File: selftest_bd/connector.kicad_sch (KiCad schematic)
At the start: 209 parts, among them J1 9001-14961C00A, J2 9001-14961C00A

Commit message: Commit V2.0
Redo PCB due to incorrect position of J1 and J2
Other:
- title: FIRST TEST STATION SELFTEST BOARD 640-1010-010 -> FIRST TEST STATION SELFTEST BOARD 640-1010-020
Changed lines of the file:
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@@
   (paper "A")
   (title_block
-    (title "FIRST TEST STATION SELFTEST BOARD 640-1010-010")
-    (date "2023-05-16")
-    (rev "1.0")
+    (title "FIRST TEST STATION SELFTEST BOARD 640-1010-020")
+    (date "2023-10-01")
+    (rev "2.0")
   )
   (junction (at 25.4 96.52) (diameter 0) (color 0 0 0 0)

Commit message: update README and small correction
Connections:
- net PM1_IO8 renamed PM1_IO0
- net PM1_IO9 renamed PM1_IO1
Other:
- title: FIRST TEST STATION SELFTEST BOARD 640-1010-020 -> FIRST TEST STATION SELFTEST BOARD 640-1010-021
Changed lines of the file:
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@@
   (paper "A")
   (title_block
-    (title "FIRST TEST STATION SELFTEST BOARD 640-1010-020")
+    (title "FIRST TEST STATION SELFTEST BOARD 640-1010-021")
     (date "2023-10-01")
-    (rev "2.0")
+    (rev "2.1")
   )
   (junction (at 25.4 96.52) (diameter 0) (color 0 0 0 0)
@@
     )
   )
-  (global_label "PM1_IO9" (shape bidirectional) (at 109.22 91.44 0) (fields_autoplaced)
-    (effects (font (size 1.27 1.27)) (justify left))
-    (property "Intersheetrefs" "${INTERSHEET_REFS}" (at 119.6764 91.3606 0)
+  (global_label "PM1_IO1" (shape bidirectional) (at 109.22 91.44 0) (fields_autoplaced)
+    (effects (font (size 1.27 1.27)) (justify left))
+    (property "Intersheetrefs" "${INTERSHEET_REFS}" (at 121.2804 91.44 0)
       (effects (font (size 1.27 1.27)) (justify left) hide)
     )
@@
     )
   )
-  (global_label "PM1_IO8" (shape bidirectional) (at 43.18 134.62 180) (fields_autoplaced)
-    (effects (font (size 1.27 1.27)) (justify right))
-    (property "Intersheetrefs" "${INTERSHEET_REFS}" (at 32.7236 134.5406 0)
-      (effects (font (size 1.27 1.27)) (justify right) hide)
-    )
+  (global_label "PM1_IO0" (shape bidirectional) (at 43.18 134.62 180) (fields_autoplaced)
+    (effects (font (size 1.27 1.27)) (justify right))
+    (property "Intersheetrefs" "${INTERSHEET_REFS}" (at 31.1196 134.62 0)
+      (effects (font (size 1.27 1.27)) (justify right) hide)
+    )

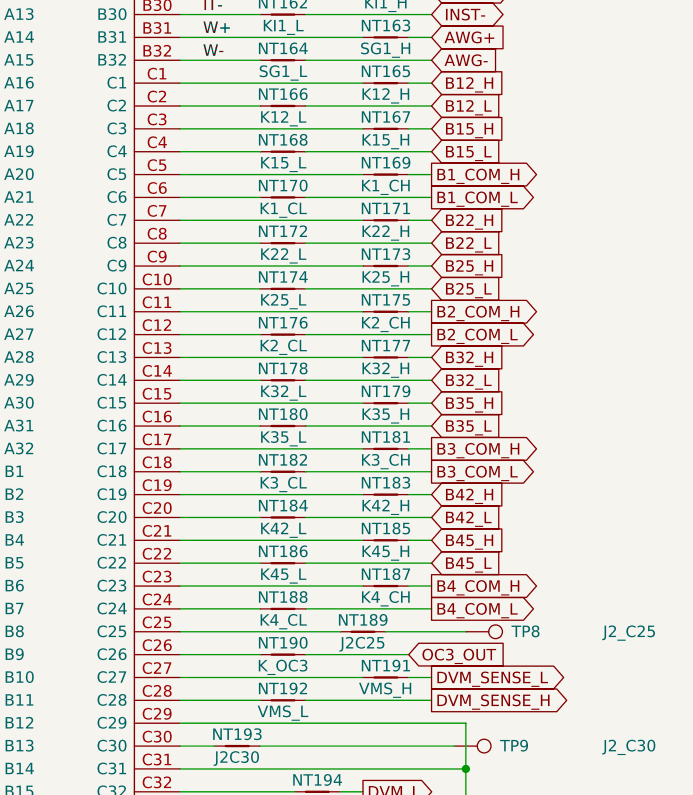
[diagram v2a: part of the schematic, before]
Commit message: Reverse COM_H and COM_L on relay Bank
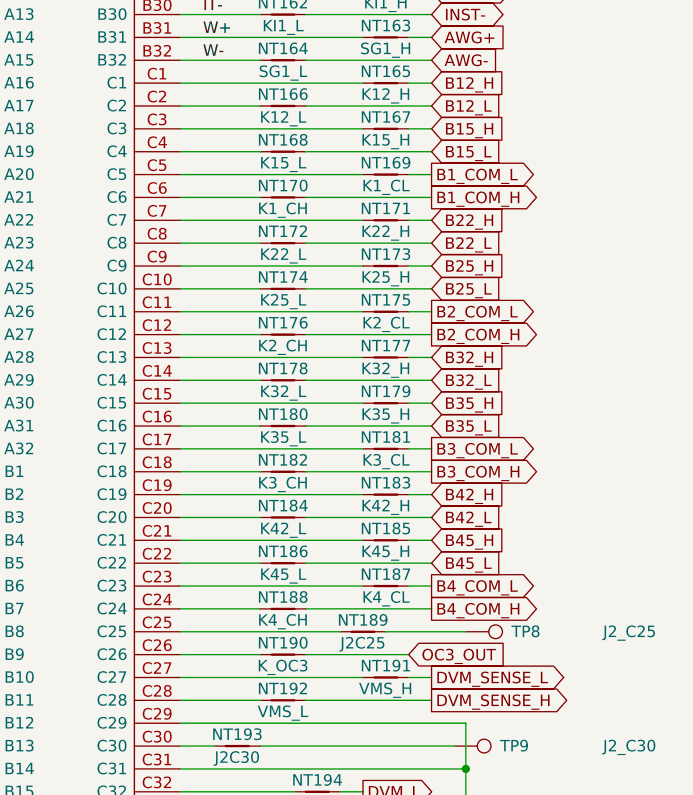
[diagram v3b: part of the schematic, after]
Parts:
- NT169: value K1_CH -> K1_CL
- NT170: value K1_CL -> K1_CH
- NT175: value K2_CH -> K2_CL
- NT176: value K2_CL -> K2_CH
- NT181: value K3_CH -> K3_CL
- NT182: value K3_CL -> K3_CH
- NT187: value K4_CH -> K4_CL
- NT188: value K4_CL -> K4_CH
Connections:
- net B1_COM_H: now also NT170.1; no longer NT169.1
- net B1_COM_L: now also NT169.1; no longer NT170.1
- net B2_COM_H: now also NT176.1; no longer NT175.1
- net B2_COM_L: now also NT175.1; no longer NT176.1
- net B3_COM_H: now also NT182.2; no longer NT181.2
- net B3_COM_L: now also NT181.2; no longer NT182.2
- net B4_COM_H: now also NT188.1; no longer NT187.1
- net B4_COM_L: now also NT187.1; no longer NT188.1
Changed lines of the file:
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@@
     )
   )
-  (global_label "B4_COM_H" (shape output) (at 238.76 129.54 0) (fields_autoplaced)
+  (global_label "B4_COM_L" (shape output) (at 238.76 129.54 0) (fields_autoplaced)
     (effects (font (size 1.27 1.27)) (justify left))
-    (property "Intersheetrefs" "${INTERSHEET_REFS}" (at 250.9702 129.4606 0)
+    (property "Intersheetrefs" "${INTERSHEET_REFS}" (at 251.1605 129.54 0)
       (effects (font (size 1.27 1.27)) (justify left) hide)
     )
@@
     )
   )
-  (global_label "B3_COM_L" (shape output) (at 238.76 116.84 0) (fields_autoplaced)
+  (global_label "B3_COM_H" (shape output) (at 238.76 116.84 0) (fields_autoplaced)
     (effects (font (size 1.27 1.27)) (justify left))
-    (property "Intersheetrefs" "${INTERSHEET_REFS}" (at 250.6679 116.7606 0)
+    (property "Intersheetrefs" "${INTERSHEET_REFS}" (at 251.4629 116.84 0)
       (effects (font (size 1.27 1.27)) (justify left) hide)
     )
@@
     )
   )
-  (global_label "B3_COM_H" (shape output) (at 238.76 114.3 0) (fields_autoplaced)
+  (global_label "B3_COM_L" (shape output) (at 238.76 114.3 0) (fields_autoplaced)
     (effects (font (size 1.27 1.27)) (justify left))
-    (property "Intersheetrefs" "${INTERSHEET_REFS}" (at 250.9702 114.2206 0)
+    (property "Intersheetrefs" "${INTERSHEET_REFS}" (at 251.1605 114.3 0)
       (effects (font (size 1.27 1.27)) (justify left) hide)
     )
@@
     )
   )
-  (global_label "B4_COM_L" (shape output) (at 238.76 132.08 0) (fields_autoplaced)
+  (global_label "B4_COM_H" (shape output) (at 238.76 132.08 0) (fields_autoplaced)
     (effects (font (size 1.27 1.27)) (justify left))
-    (property "Intersheetrefs" "${INTERSHEET_REFS}" (at 250.6679 132.0006 0)
+    (property "Intersheetrefs" "${INTERSHEET_REFS}" (at 251.4629 132.08 0)
       (effects (font (size 1.27 1.27)) (justify left) hide)
     )
@@
     )
   )
-  (global_label "B1_COM_H" (shape output) (at 238.76 83.82 0) (fields_autoplaced)
+  (global_label "B1_COM_L" (shape output) (at 238.76 83.82 0) (fields_autoplaced)
     (effects (font (size 1.27 1.27)) (justify left))
-    (property "Intersheetrefs" "${INTERSHEET_REFS}" (at 250.9702 83.7406 0)
+    (property "Intersheetrefs" "${INTERSHEET_REFS}" (at 251.1605 83.82 0)
       (effects (font (size 1.27 1.27)) (justify left) hide)
     )
@@
     )
   )
-  (global_label "B2_COM_H" (shape output) (at 238.76 99.06 0) (fields_autoplaced)
+  (global_label "B2_COM_L" (shape output) (at 238.76 99.06 0) (fields_autoplaced)
     (effects (font (size 1.27 1.27)) (justify left))
-    (property "Intersheetrefs" "${INTERSHEET_REFS}" (at 250.9702 98.9806 0)
+    (property "Intersheetrefs" "${INTERSHEET_REFS}" (at 251.1605 99.06 0)
       (effects (font (size 1.27 1.27)) (justify left) hide)
     )
@@
     )
   )
-  (global_label "B2_COM_L" (shape output) (at 238.76 101.6 0) (fields_autoplaced)
+  (global_label "B2_COM_H" (shape output) (at 238.76 101.6 0) (fields_autoplaced)
     (effects (font (size 1.27 1.27)) (justify left))
-    (property "Intersheetrefs" "${INTERSHEET_REFS}" (at 250.6679 101.5206 0)
+    (property "Intersheetrefs" "${INTERSHEET_REFS}" (at 251.4629 101.6 0)
       (effects (font (size 1.27 1.27)) (justify left) hide)
     )
@@
     )
   )
-  (global_label "B1_COM_L" (shape output) (at 238.76 86.36 0) (fields_autoplaced)
+  (global_label "B1_COM_H" (shape output) (at 238.76 86.36 0) (fields_autoplaced)
     (effects (font (size 1.27 1.27)) (justify left))
-    (property "Intersheetrefs" "${INTERSHEET_REFS}" (at 250.6679 86.2806 0)
+    (property "Intersheetrefs" "${INTERSHEET_REFS}" (at 251.4629 86.36 0)
       (effects (font (size 1.27 1.27)) (justify left) hide)
     )
@@
       (effects (font (size 1.27 1.27)))
     )
-    (property "Value" "K1_CL" (at 222.25 87.63 0)
+    (property "Value" "K1_CH" (at 222.25 87.63 0)
       (effects (font (size 1.27 1.27)))
     )
@@
       (effects (font (size 1.27 1.27)))
     )
-    (property "Value" "K3_CH" (at 233.68 115.57 0)
+    (property "Value" "K3_CL" (at 233.68 115.57 0)
       (effects (font (size 1.27 1.27)))
     )
@@
       (effects (font (size 1.27 1.27)))
     )
-    (property "Value" "K4_CL" (at 222.25 133.35 0)
+    (property "Value" "K4_CH" (at 222.25 133.35 0)
       (effects (font (size 1.27 1.27)))
     )
@@
       (effects (font (size 1.27 1.27)))
     )
-    (property "Value" "K3_CL" (at 222.25 118.11 0)
+    (property "Value" "K3_CH" (at 222.25 118.11 0)
       (effects (font (size 1.27 1.27)))
     )
@@
       (effects (font (size 1.27 1.27)))
     )
-    (property "Value" "K2_CL" (at 222.25 102.87 0)
+    (property "Value" "K2_CH" (at 222.25 102.87 0)
       (effects (font (size 1.27 1.27)))
     )
@@
       (effects (font (size 1.27 1.27)))
     )
-    (property "Value" "K1_CH" (at 233.68 85.09 0)
+    (property "Value" "K1_CL" (at 233.68 85.09 0)
       (effects (font (size 1.27 1.27)))
     )
@@
       (effects (font (size 1.27 1.27)))
     )
-    (property "Value" "K4_CH" (at 233.68 130.81 0)
+    (property "Value" "K4_CL" (at 233.68 130.81 0)
       (effects (font (size 1.27 1.27)))
     )
@@
       (effects (font (size 1.27 1.27)))
     )
-    (property "Value" "K2_CH" (at 233.68 100.33 0)
+    (property "Value" "K2_CL" (at 233.68 100.33 0)
       (effects (font (size 1.27 1.27)))
     )
